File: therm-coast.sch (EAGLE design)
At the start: 2 parts, among them U1 ATTINY85-20SU

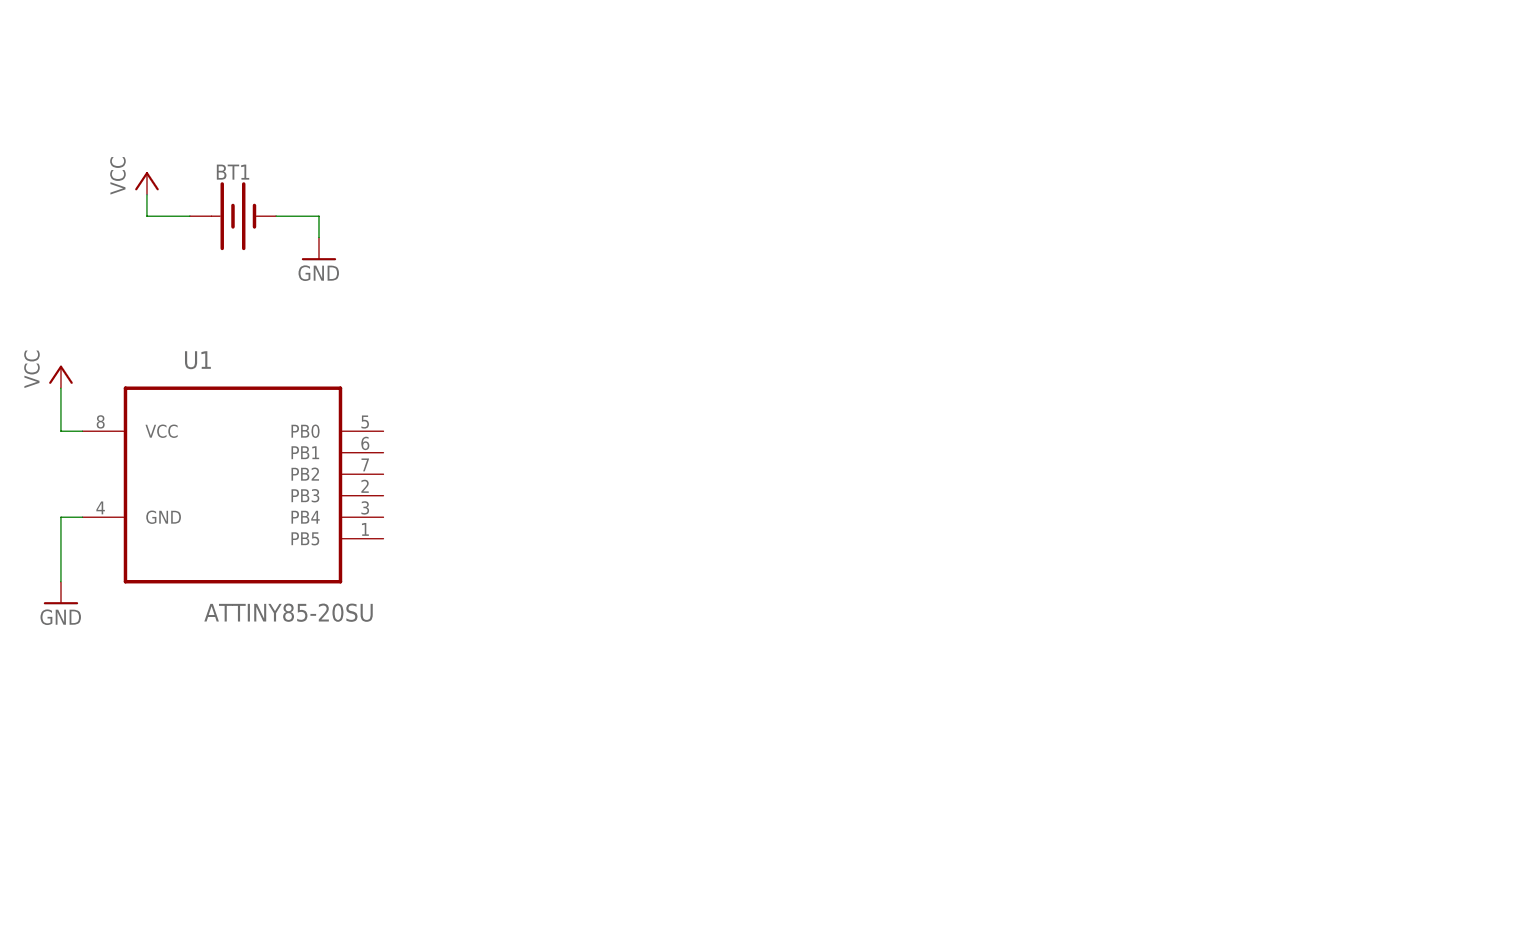
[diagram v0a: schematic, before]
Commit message: Schematic Design
Added major components including LEDs, Thermsistor and some power regulation
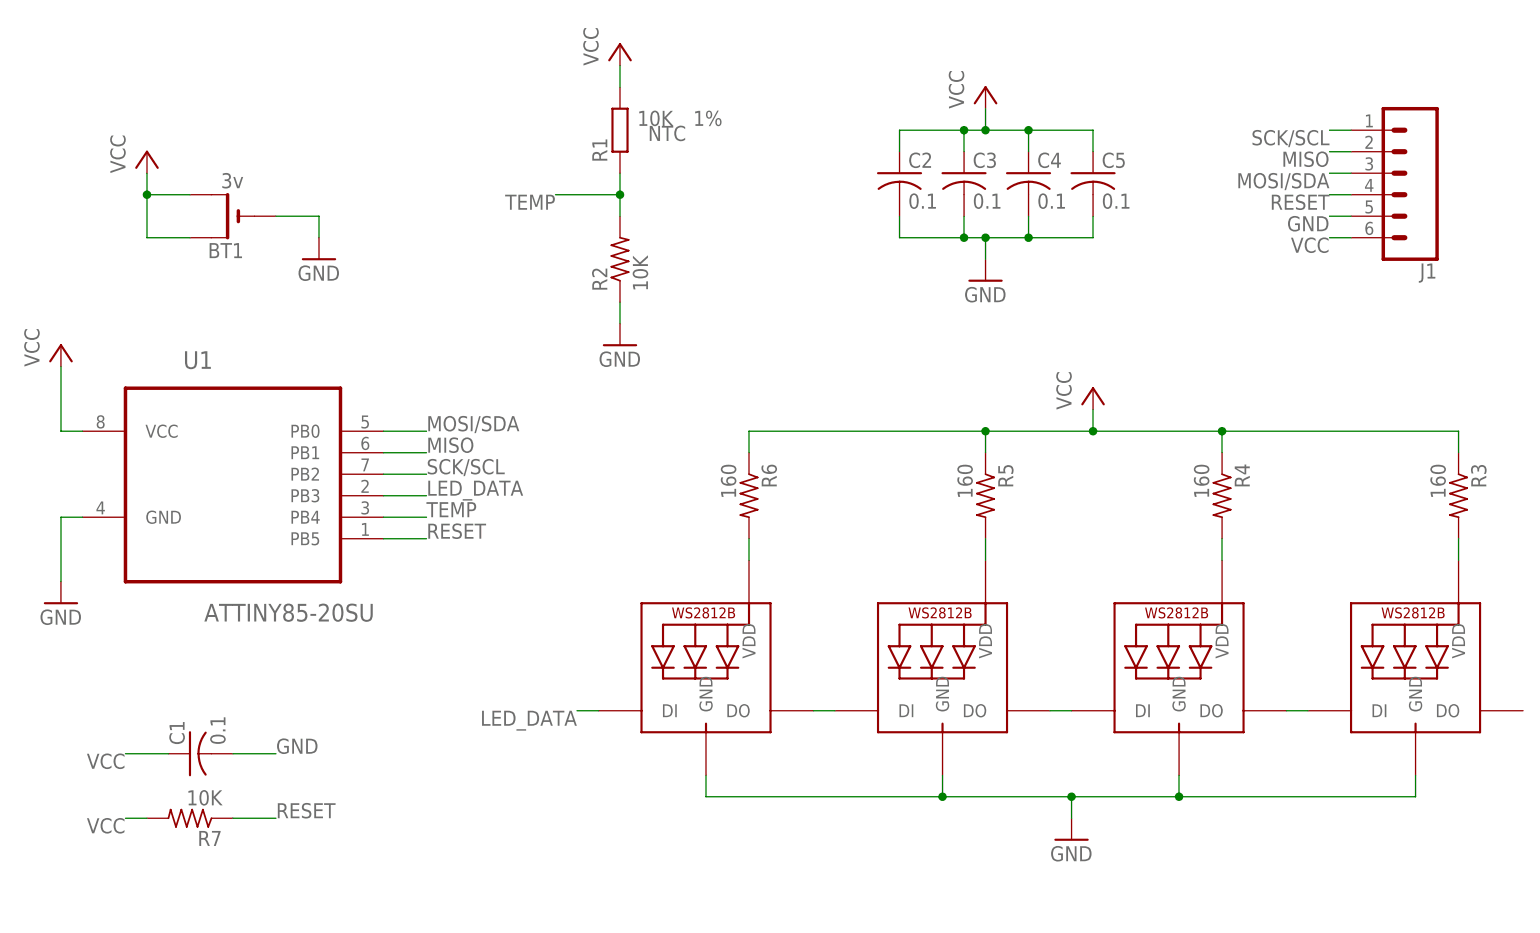
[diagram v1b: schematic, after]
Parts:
- added C1, C2, C3, C4, C5: 0.1, resistor:C-USC0805
- added J1: (no value), SparkFun-Connectors:CONN_06SMD-FEMALE-V2
- added LED1, LED2, LED3, LED4: WS2812B5050, Adafruit:WS2812B5050
- added R1: 10K, resistor:R-EU_R0805
- added R2, R7: 10K, resistor:R-US_R0805
- added R3, R4, R5, R6: 160, resistor:R-US_R0805
- BT1: value (none) -> 3v; device SparkFun-Batteries:BATTERY-20MM_SMD -> Adafruit:CR2032SMT
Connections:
- new net LED_DATA: LED1.DI, U1.PB3
- new net MISO: J1.2, U1.PB1
- new net MOSI/SDA: J1.3, U1.PB0
- new net N$1: LED1.VDD, R6.2
- new net N$2: LED2.VDD, R5.2
- new net N$3: LED3.VDD, R4.2
- new net N$4: LED4.VDD, R3.2
- new net N$5: LED1.DO, LED2.DI
- new net N$6: LED2.DO, LED3.DI
- new net N$7: LED3.DO, LED4.DI
- new net RESET: J1.4, R7.1, U1.PB5
- new net SCK/SCL: J1.1, U1.PB2
- new net TEMP: R1.1, R2.2, U1.PB4
- net GND: now also C1.2, C2.2, C3.2, C4.2, C5.2, J1.5, LED1.GND, LED2.GND, LED3.GND, LED4.GND, R2.1
- net VCC: now also BT1.+1, C1.1, C2.1, C3.1, C4.1, C5.1, J1.6, R1.2, R3.1, R4.1, R5.1, R6.1, R7.2

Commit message: Board Placement and Routing updates
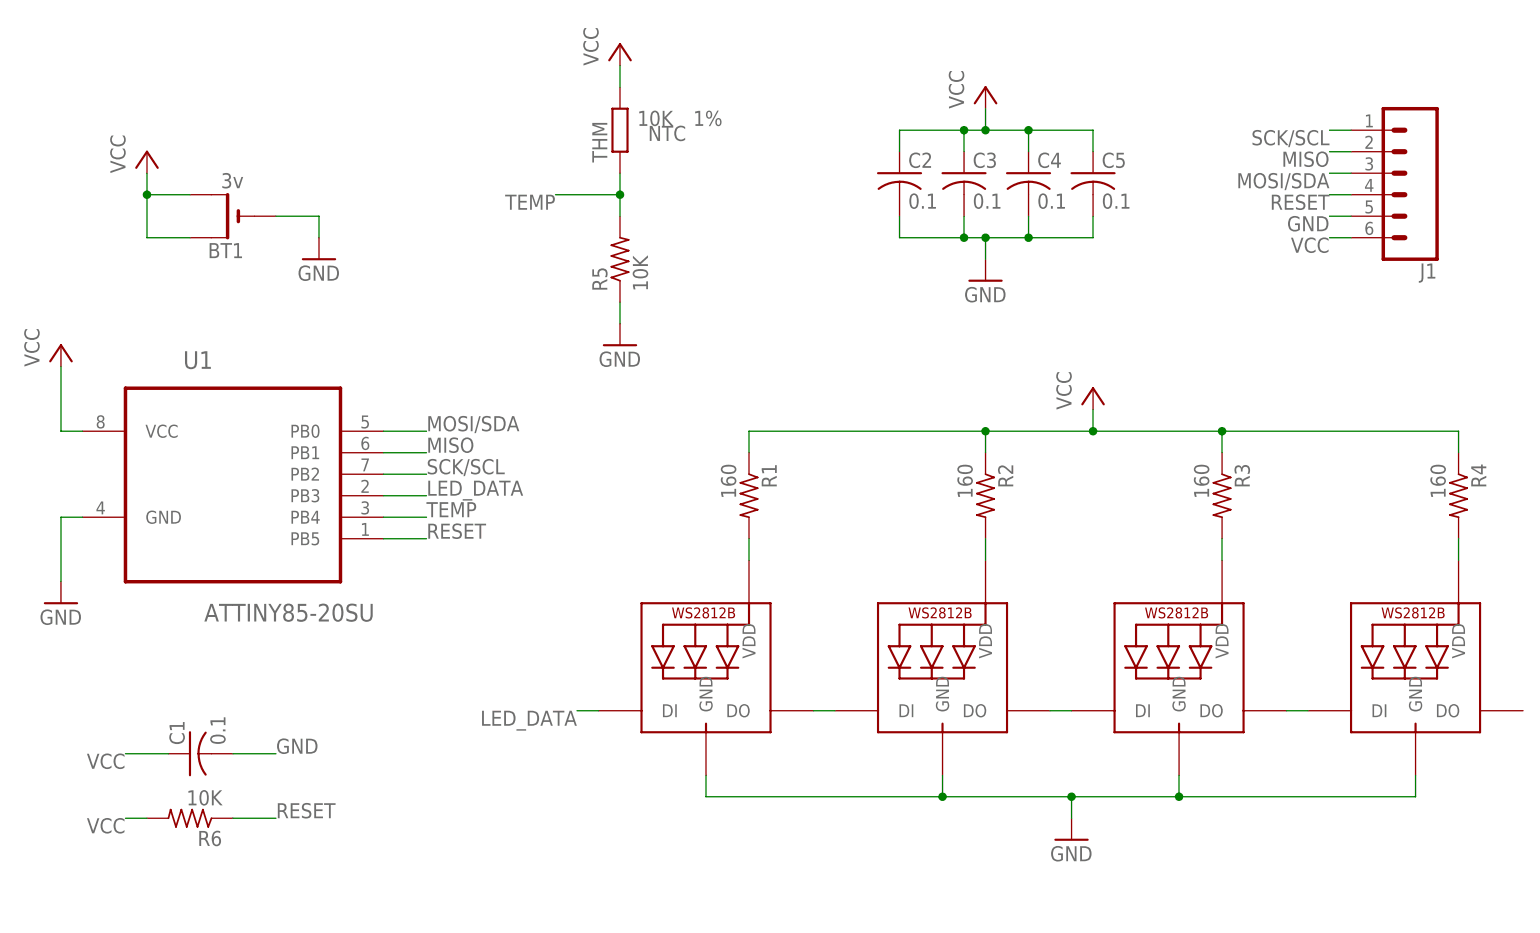
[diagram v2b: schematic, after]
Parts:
- removed R7: 10K, resistor:R-US_R0805
- added THM: 10K, resistor:R-EU_R0805
- R1: value 10K -> 160; device resistor:R-EU_R0805 -> resistor:R-US_R0805; TOLERANCE 1% -> (none); TYPE NTC -> (none)
- R2: value 10K -> 160
- R5, R6: value 160 -> 10K
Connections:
- net GND: now also R5.1; no longer R2.1
- net N$1: now also R1.2; no longer R6.2
- net N$2: now also R2.2; no longer R5.2
- net N$3: now also R3.2; no longer R4.2
- net N$4: now also R4.2; no longer R3.2
- net RESET: now also R6.1; no longer R7.1
- net TEMP: now also R5.2, THM.1; no longer R1.1, R2.2
- net VCC: now also R1.1, R2.1, R6.2, THM.2; no longer R1.2, R5.1, R6.1, R7.2
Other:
- moved on the sheet: R2, R3, R4, R5, R6
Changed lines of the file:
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@@
 </variantdefs>
 <classes>
-<class number="0" name="default" width="0" drill="0">
+<class number="0" name="default" width="0.8128" drill="0">
 </class>
 </classes>
@@
 <part name="P+2" library="supply1" deviceset="VCC" device=""/>
 <part name="GND2" library="supply1" deviceset="GND" device=""/>
-<part name="R1" library="resistor" deviceset="R-EU_" device="R0805" value="10K">
+<part name="THM" library="resistor" deviceset="R-EU_" device="R0805" value="10K">
 <attribute name="TOLERANCE" value="1%"/>
 <attribute name="TYPE" value="NTC"/>
 </part>
-<part name="R2" library="resistor" deviceset="R-US_" device="R0805" value="10K"/>
+<part name="R5" library="resistor" deviceset="R-US_" device="R0805" value="10K"/>
 <part name="P+3" library="supply1" deviceset="VCC" device=""/>
 <part name="P+4" library="supply1" deviceset="VCC" device=""/>
@@
 <part name="GND3" library="supply1" deviceset="GND" device=""/>
 <part name="GND5" library="supply1" deviceset="GND" device=""/>
+<part name="R4" library="resistor" deviceset="R-US_" device="R0805" value="160"/>
 <part name="R3" library="resistor" deviceset="R-US_" device="R0805" value="160"/>
-<part name="R4" library="resistor" deviceset="R-US_" device="R0805" value="160"/>
-<part name="R5" library="resistor" deviceset="R-US_" device="R0805" value="160"/>
-<part name="R6" library="resistor" deviceset="R-US_" device="R0805" value="160"/>
+<part name="R2" library="resistor" deviceset="R-US_" device="R0805" value="160"/>
+<part name="R1" library="resistor" deviceset="R-US_" device="R0805" value="160"/>
 <part name="LED1" library="Adafruit" deviceset="WS2812B" device="5050"/>
 <part name="LED2" library="Adafruit" deviceset="WS2812B" device="5050"/>
@@
 <part name="LED4" library="Adafruit" deviceset="WS2812B" device="5050"/>
 <part name="P+5" library="supply1" deviceset="VCC" device=""/>
-<part name="R7" library="resistor" deviceset="R-US_" device="R0805" value="10K"/>
+<part name="R6" library="resistor" deviceset="R-US_" device="R0805" value="10K"/>
 <part name="J1" library="SparkFun-Connectors" deviceset="CONN_06" device="SMD-FEMALE-V2"/>
 </parts>
@@
 <instance part="P+2" gate="VCC" x="27.94" y="96.52"/>
 <instance part="GND2" gate="1" x="48.26" y="83.82"/>
-<instance part="R1" gate="G$1" x="83.82" y="99.06" smashed="yes" rot="R90">
+<instance part="THM" gate="G$1" x="83.82" y="99.06" smashed="yes" rot="R90">
 <attribute name="TYPE" x="87.122" y="97.79" size="1.778" layer="96"/>
 <attribute name="TOLERANCE" x="92.456" y="99.568" size="1.778" layer="96"/>
@@
 <attribute name="VALUE" x="85.852" y="99.568" size="1.778" layer="96"/>
 </instance>
-<instance part="R2" gate="G$1" x="83.82" y="83.82" rot="R90"/>
+<instance part="R5" gate="G$1" x="83.82" y="83.82" rot="R90"/>
 <instance part="P+3" gate="VCC" x="83.82" y="109.22"/>
 <instance part="P+4" gate="VCC" x="127" y="104.14"/>
@@
 <instance part="GND3" gate="1" x="83.82" y="73.66"/>
 <instance part="GND5" gate="1" x="137.16" y="15.24"/>
-<instance part="R3" gate="G$1" x="182.88" y="55.88" rot="R270"/>
-<instance part="R4" gate="G$1" x="154.94" y="55.88" rot="R270"/>
-<instance part="R5" gate="G$1" x="127" y="55.88" rot="R270"/>
-<instance part="R6" gate="G$1" x="99.06" y="55.88" rot="R270"/>
+<instance part="R4" gate="G$1" x="182.88" y="55.88" rot="R270"/>
+<instance part="R3" gate="G$1" x="154.94" y="55.88" rot="R270"/>
+<instance part="R2" gate="G$1" x="127" y="55.88" rot="R270"/>
+<instance part="R1" gate="G$1" x="99.06" y="55.88" rot="R270"/>
 <instance part="LED1" gate="G$1" x="93.98" y="33.02"/>
 <instance part="LED2" gate="G$1" x="121.92" y="33.02"/>
@@
 <instance part="LED4" gate="G$1" x="177.8" y="33.02"/>
 <instance part="P+5" gate="VCC" x="139.7" y="68.58"/>
-<instance part="R7" gate="G$1" x="33.02" y="17.78" rot="R180"/>
+<instance part="R6" gate="G$1" x="33.02" y="17.78" rot="R180"/>
 <instance part="J1" gate="G$1" x="175.26" y="93.98" rot="R180"/>
 </instances>
@@
 </segment>
 <segment>
-<pinref part="R1" gate="G$1" pin="2"/>
+<pinref part="THM" gate="G$1" pin="2"/>
 <wire x1="83.82" y1="106.68" x2="83.82" y2="104.14" width="0.1524" layer="91"/>
 <pinref part="P+3" gate="VCC" pin="VCC"/>
@@
 </segment>
 <segment>
-<pinref part="R6" gate="G$1" pin="1"/>
+<pinref part="R1" gate="G$1" pin="1"/>
 <wire x1="182.88" y1="63.5" x2="154.94" y2="63.5" width="0.1524" layer="91"/>
 <wire x1="154.94" y1="63.5" x2="139.7" y2="63.5" width="0.1524" layer="91"/>
@@
 <wire x1="127" y1="63.5" x2="99.06" y2="63.5" width="0.1524" layer="91"/>
 <wire x1="99.06" y1="63.5" x2="99.06" y2="60.96" width="0.1524" layer="91"/>
-<pinref part="R5" gate="G$1" pin="1"/>
+<pinref part="R2" gate="G$1" pin="1"/>
 <wire x1="127" y1="60.96" x2="127" y2="63.5" width="0.1524" layer="91"/>
 <junction x="127" y="63.5"/>
-<pinref part="R4" gate="G$1" pin="1"/>
+<pinref part="R3" gate="G$1" pin="1"/>
 <wire x1="154.94" y1="60.96" x2="154.94" y2="63.5" width="0.1524" layer="91"/>
 <junction x="154.94" y="63.5"/>
-<pinref part="R3" gate="G$1" pin="1"/>
+<pinref part="R4" gate="G$1" pin="1"/>
 <wire x1="182.88" y1="60.96" x2="182.88" y2="63.5" width="0.1524" layer="91"/>
 <pinref part="P+5" gate="VCC" pin="VCC"/>
@@
 </segment>
 <segment>
-<pinref part="R7" gate="G$1" pin="2"/>
+<pinref part="R6" gate="G$1" pin="2"/>
 <wire x1="25.4" y1="17.78" x2="27.94" y2="17.78" width="0.1524" layer="91"/>
 <label x="25.4" y="17.78" size="1.778" layer="95" rot="R180"/>
@@
 </segment>
 <segment>
-<pinref part="R2" gate="G$1" pin="1"/>
+<pinref part="R5" gate="G$1" pin="1"/>
 <wire x1="83.82" y1="78.74" x2="83.82" y2="76.2" width="0.1524" layer="91"/>
 <pinref part="GND3" gate="1" pin="GND"/>
@@
 <net name="N$1" class="0">
 <segment>
-<pinref part="R6" gate="G$1" pin="2"/>
+<pinref part="R1" gate="G$1" pin="2"/>
 <pinref part="LED1" gate="G$1" pin="VDD"/>
 <wire x1="99.06" y1="50.8" x2="99.06" y2="48.26" width="0.1524" layer="91"/>
@@
 <net name="N$2" class="0">
 <segment>
-<pinref part="R5" gate="G$1" pin="2"/>
+<pinref part="R2" gate="G$1" pin="2"/>
 <pinref part="LED2" gate="G$1" pin="VDD"/>
 <wire x1="127" y1="50.8" x2="127" y2="48.26" width="0.1524" layer="91"/>
@@
 <net name="N$3" class="0">
 <segment>
-<pinref part="R4" gate="G$1" pin="2"/>
+<pinref part="R3" gate="G$1" pin="2"/>
 <pinref part="LED3" gate="G$1" pin="VDD"/>
 <wire x1="154.94" y1="50.8" x2="154.94" y2="48.26" width="0.1524" layer="91"/>
@@
 <net name="N$4" class="0">
 <segment>
-<pinref part="R3" gate="G$1" pin="2"/>
+<pinref part="R4" gate="G$1" pin="2"/>
 <pinref part="LED4" gate="G$1" pin="VDD"/>
 <wire x1="182.88" y1="50.8" x2="182.88" y2="48.26" width="0.1524" layer="91"/>
@@
 <net name="RESET" class="0">
 <segment>
-<pinref part="R7" gate="G$1" pin="1"/>
+<pinref part="R6" gate="G$1" pin="1"/>
 <wire x1="43.18" y1="17.78" x2="38.1" y2="17.78" width="0.1524" layer="91"/>
 <label x="60.96" y="50.8" size="1.778" layer="95"/>
@@
 </segment>
 <segment>
-<pinref part="R1" gate="G$1" pin="1"/>
-<pinref part="R2" gate="G$1" pin="2"/>
+<pinref part="THM" gate="G$1" pin="1"/>
+<pinref part="R5" gate="G$1" pin="2"/>
 <wire x1="83.82" y1="93.98" x2="83.82" y2="91.44" width="0.1524" layer="91"/>
 <wire x1="83.82" y1="91.44" x2="83.82" y2="88.9" width="0.1524" layer="91"/>
@@
 </sheet>
 </sheets>
+<errors>
+</errors>
 </schematic>
 </drawing>

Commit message: Rev 1.0
Better Route and Placement, Silks
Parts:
- added LOGO1: OSHW-LOGOL, SparkFun-Aesthetics:OSHW-LOGOL
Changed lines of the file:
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@@
 <part name="R6" library="resistor" deviceset="R-US_" device="R0805" value="10K"/>
 <part name="J1" library="SparkFun-Connectors" deviceset="CONN_06" device="SMD-FEMALE-V2"/>
+<part name="LOGO1" library="SparkFun-Aesthetics" deviceset="OSHW-LOGO" device="L" value="OSHW-LOGOL"/>
 </parts>
 <sheets>
@@
 <instance part="R6" gate="G$1" x="33.02" y="17.78" rot="R180"/>
 <instance part="J1" gate="G$1" x="175.26" y="93.98" rot="R180"/>
+<instance part="LOGO1" gate="G$1" x="73.66" y="15.24"/>
 </instances>
 <busses>
